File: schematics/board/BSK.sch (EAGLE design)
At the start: 47 parts

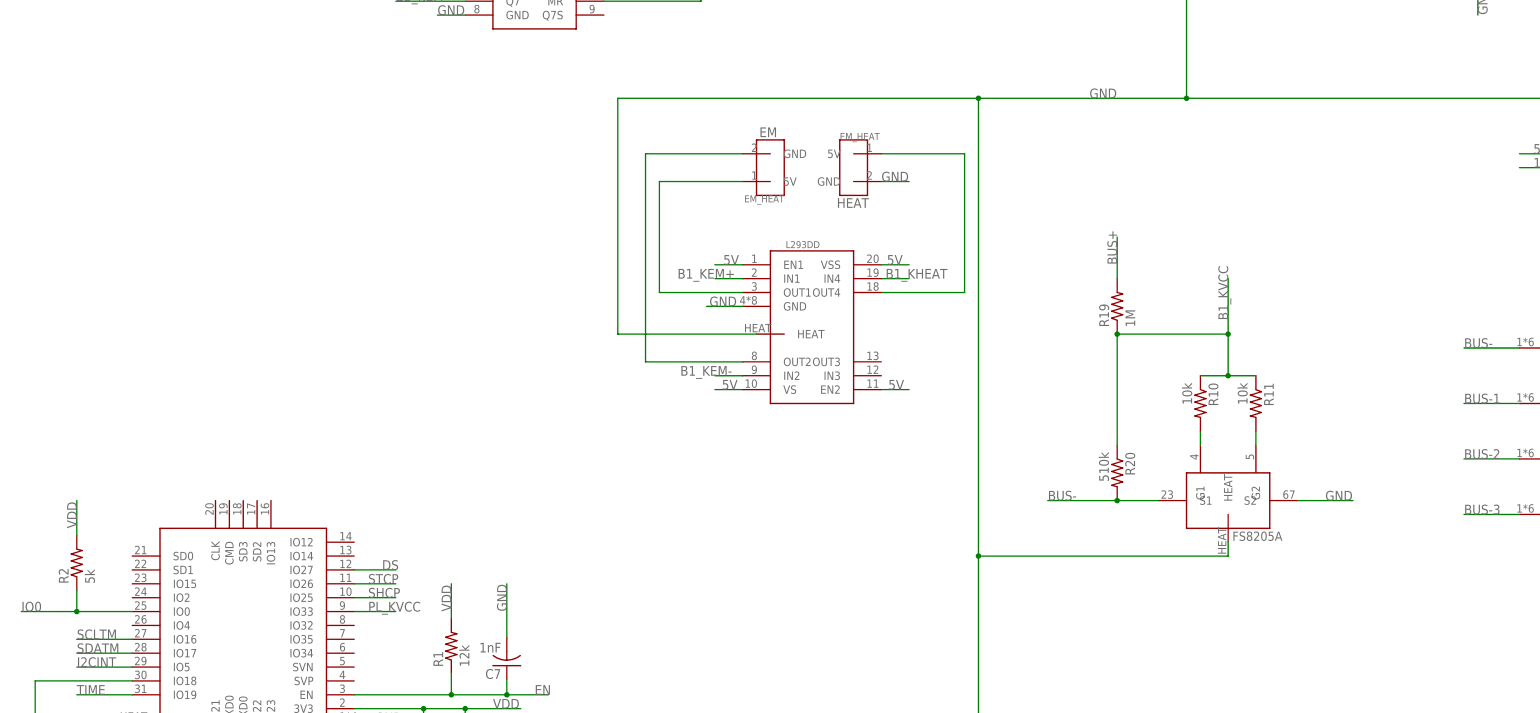
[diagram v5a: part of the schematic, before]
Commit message: Добавлены светодиоды на платы БСК
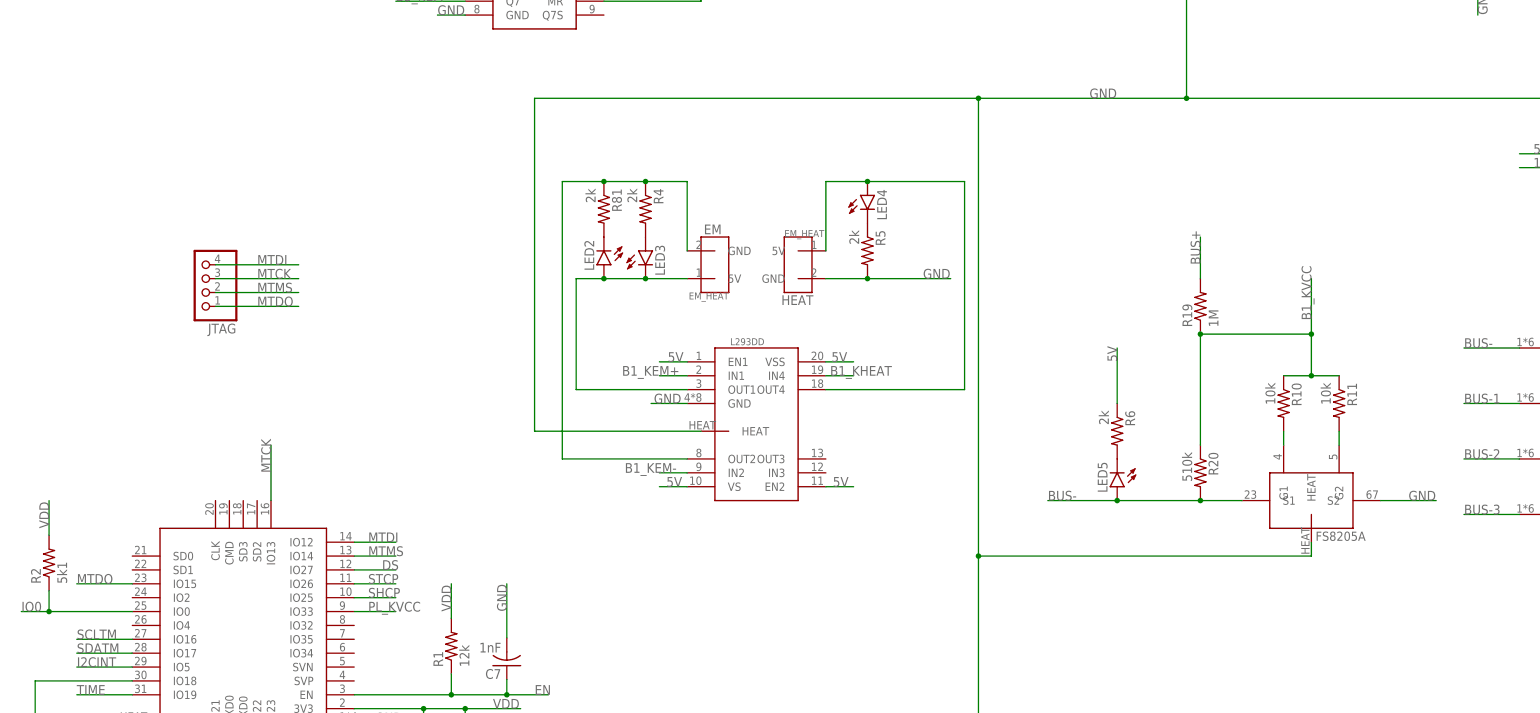
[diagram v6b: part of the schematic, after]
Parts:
- added JTAG: (no value), pinheadCS:PINHD-1X4
- added LED2, LED3, LED4, LED5: (no value), led:LEDCHIPLED_0603
- added R4, R5, R6, R81: 2k, resistor:R-US_R0603
- R2: value 5k -> 5k1
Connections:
- new net MTCK: JTAG.3, U$13.IO13
- new net MTDI: JTAG.4, U$13.IO12
- new net MTDO: JTAG.1, U$13.IO15
- new net MTMS: JTAG.2, U$13.IO14
- new net N$35: LED2.C, R81.2
- new net N$36: LED3.A, R4.2
- new net N$37: LED4.C, R5.1
- new net N$38: LED5.C, R6.2
- net 5V: now also R6.1
- net BUS-: now also LED5.A
- net GND: now also R5.2
- net N$1: now also LED2.A, LED3.C
- net N$2: now also R4.1, R81.1
- net N$3: now also LED4.A
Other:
- moved on the sheet: R10, R11, R19, R2, R20

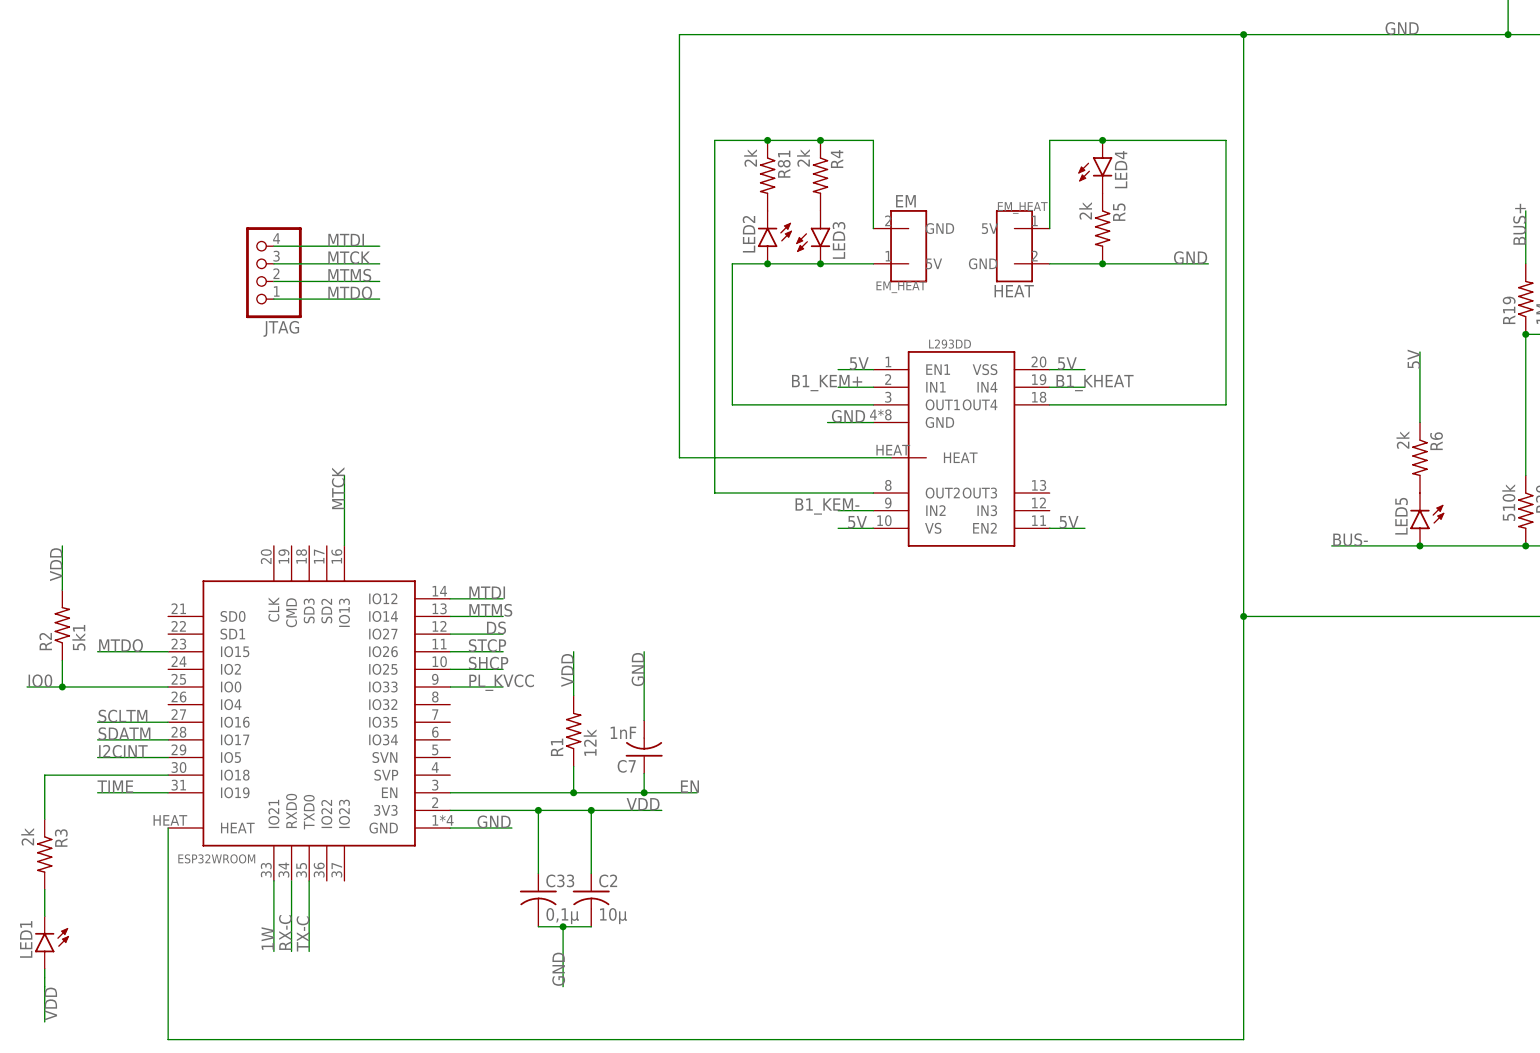
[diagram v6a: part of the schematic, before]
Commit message: Посмотрел плату БСК1, немного поправил и разместил шелкографию
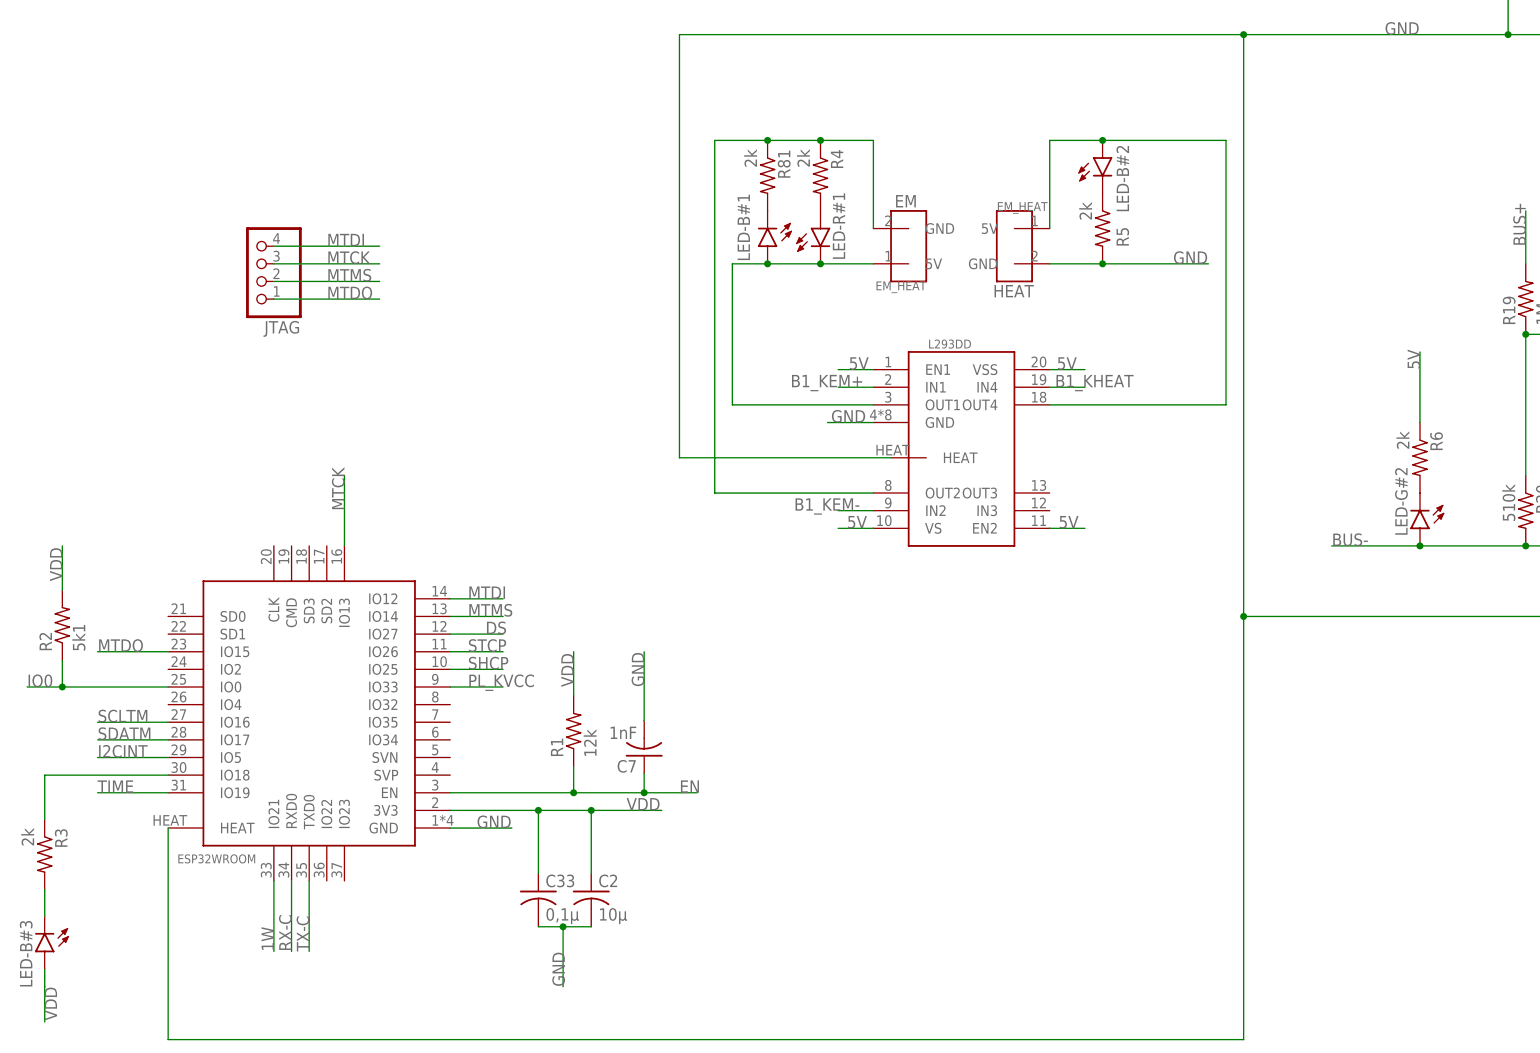
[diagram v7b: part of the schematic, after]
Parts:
- USB-C: SPICEPREFIX (none) -> X
- renumbered LED1 to LED-B#3, LED2 to LED-B#1, LED3 to LED-R#1, LED4 to LED-B#2, LED5 to LED-G#2, U$10 to LTC3633, U$11 to B82498F#1, U$12 to B82498F#2, U$15 to 74HC595#2, U$16 to USB-C, U$17 to 74HC595#3, U$22 to FS8205A, U$5 to DS18B20Z, U$6 to EM, U$7 to HEATER, U$8 to L293DD, U$9 to 74HC595#1
